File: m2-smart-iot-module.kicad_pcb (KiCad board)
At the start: 4 copper layers, 80.2 x 22.1 mm, 200 parts, among them IC1 UPD720201K8-711-BAC-A, J1 MM8130-2600RA2, J2 2X05, J3 M.2-M+B-Pins, Q1 BSS123, SW1 PTS840_GK_SMTR_LFS, SW2 PTS840_GK_SMTR_LFS, U1 FT2232H-56Q, U10 MIC2877-5.0YFT-TR, U11 93LC56CT-IMC, U2 SST25VF512A, U3 CoralAccelerator, U4 NRF52840, U5 AP2120N-1.8TRG1, U6 AP22652W6-7, U7 TLV803EF29DBZR, U8 BME280, U9 NCP1599MNTWG, Y1 NX3225SA-24M, Y2 ABM11W-101-32.0000MHZ-T3, Y3 ABS06-32.768KHZ-9-1-T, Y4 ABM8G-12M-18-D2Y-T

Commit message: Fix DRC
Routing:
- net 3V3: track 153.4 -> 152.0 mm
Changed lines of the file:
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@@
   (paper "A4")
   (title_block
-    (date "2022-07-15")
+    (date "2022-07-18")
     (rev "1.2.4")
   )
@@
   (via (at 145.41 99.52) (size 0.6) (drill 0.3) (layers "F.Cu" "B.Cu") (free) (net 1))
   (via (at 149.575 95.975) (size 0.5) (drill 0.2) (layers "F.Cu" "B.Cu") (free) (net 1))
-  (via (at 135.2 105.2) (size 0.6) (drill 0.3) (layers "F.Cu" "B.Cu") (free) (net 1))
+  (via (at 134.85 105.55) (size 0.6) (drill 0.3) (layers "F.Cu" "B.Cu") (free) (net 1))
   (via (at 177.8 92.2) (size 0.6) (drill 0.3) (layers "F.Cu" "B.Cu") (free) (net 1))
   (via (at 132.08 96.774) (size 0.6) (drill 0.3) (layers "F.Cu" "B.Cu") (net 1))
@@
   (segment (start 188.225 95.5) (end 188.3 95.575) (width 0.5) (layer "F.Cu") (net 2))
   (segment (start 135.372501 110.825) (end 135.45 110.902499) (width 0.35) (layer "F.Cu") (net 2))
-  (segment (start 186.03 98.135) (end 186.03 99.543) (width 0.5) (layer "F.Cu") (net 2))
   (segment (start 160.875 105.6) (end 158.95 105.6) (width 0.35) (layer "F.Cu") (net 2))
   (segment (start 135.087503 109.525) (end 135.45 109.887497) (width 0.35) (layer "F.Cu") (net 2))
@@
   (segment (start 187.338 107.798536) (end 188.214 107.798536) (width 0.128) (layer "F.Cu") (net 40))
   (segment (start 182.588 103.848536) (end 182.588 103.438283) (width 0.128) (layer "F.Cu") (net 40))
-  (segment (start 181.987 98.171) (end 181.811 97.995) (width 0.2) (layer "F.Cu") (net 40))
   (segment (start 183.388 112.224502) (end 183.388 111.748536) (width 0.128) (layer "F.Cu") (net 40))
   (segment (start 179.438 108.998536) (end 178.379119 108.998536) (width 0.128) (layer "F.Cu") (net 40))
@@
       (pts
         (xy 192.039 109.092671)
-        (xy 189.322 109.093)
-        (xy 189.322 111.506)
+        (xy 188.772 109.093)
+        (xy 188.772 111.506)
         (xy 185.039 111.506)
         (xy 185.038987 113.523394)

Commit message: Bump revision to 1.2.5
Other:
- board text added: "rev 1.2.5"
- board text removed: "rev 1.2.4"
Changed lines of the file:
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@@
   (title_block
     (date "2022-07-18")
-    (rev "1.2.4")
+    (rev "1.2.5")
   )
   (layers
@@
     (effects (font (size 0.65 0.65) (thickness 0.15)) (justify mirror))
   )
-  (gr_text "rev 1.2.4" (at 185.928 94.05) (layer "B.Mask")
+  (gr_text "rev 1.2.5" (at 185.928 94.05) (layer "B.Mask")
     (effects (font (size 0.65 0.65) (thickness 0.15)) (justify mirror))
   )

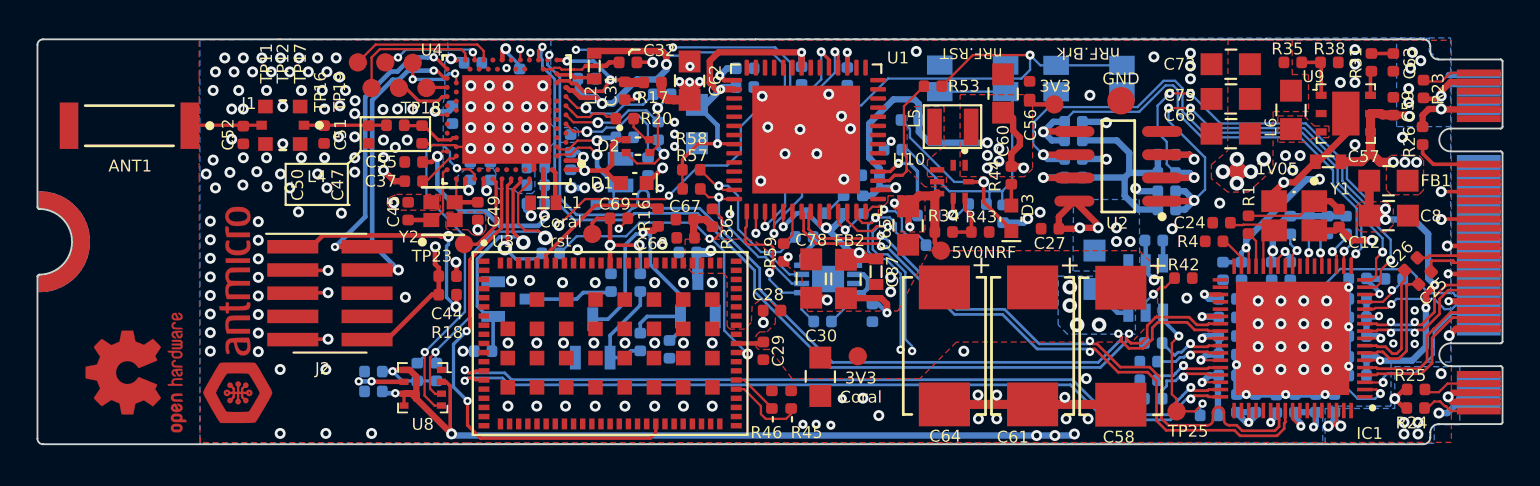
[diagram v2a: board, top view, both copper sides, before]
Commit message: Place NRF52 reset via in empty space between AC9 and AC5
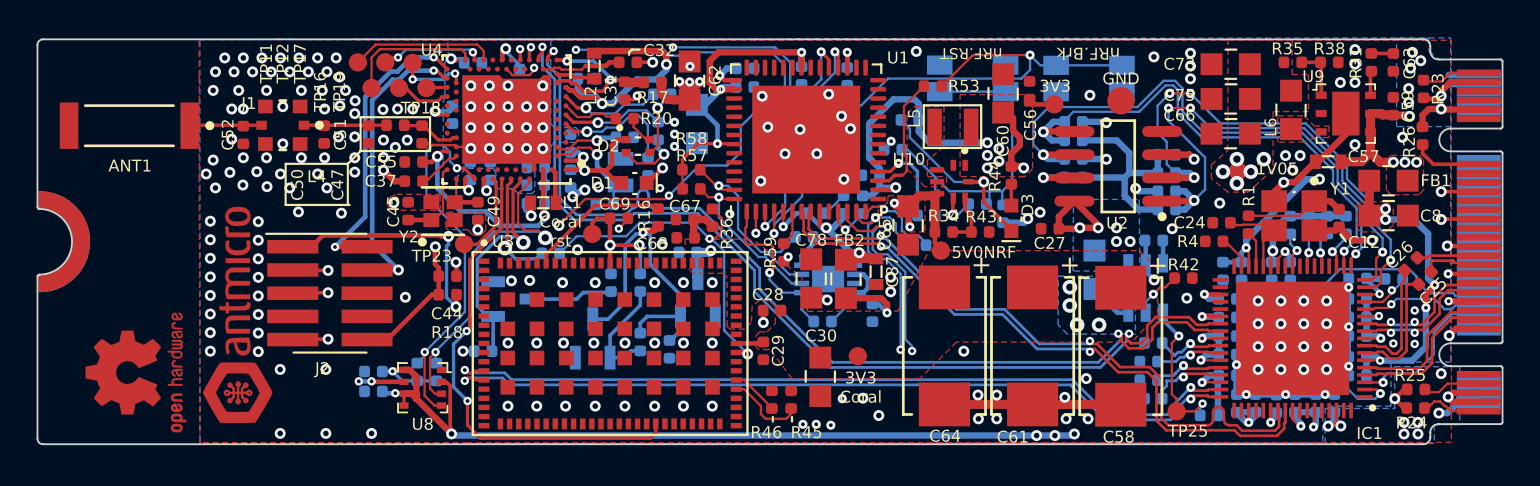
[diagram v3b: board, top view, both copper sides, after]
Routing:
- net /nRF52840/~{RESET}: track 69.3 -> 78.7 mm
- net /nRF52840/LED2_R: track 5.76 -> 7.68 mm
- net Radio_USB_N: track 53.4 -> 54.0 mm

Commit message: Bump revision to 1.2.6
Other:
- board text added: "rev 1.2.6"
- board text removed: "rev 1.2.5"
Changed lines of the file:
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@@
   (paper "A4")
   (title_block
-    (date "2022-07-18")
-    (rev "1.2.5")
+    (date "2022-07-19")
+    (rev "1.2.6")
   )
   (layers
@@
     (effects (font (size 0.65 0.65) (thickness 0.15)) (justify mirror))
   )
-  (gr_text "rev 1.2.5" (at 185.928 94.05) (layer "B.Mask")
+  (gr_text "rev 1.2.6" (at 185.928 94.05) (layer "B.Mask")
     (effects (font (size 0.65 0.65) (thickness 0.15)) (justify mirror))
   )
